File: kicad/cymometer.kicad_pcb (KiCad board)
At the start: 2 copper layers, 128.4 x 62 mm, 60 parts, among them IC1 ATMEGA8-P, P1 BNC, P2 CONN_2, P3 CONN_3X2, Q1 BC550, SW1 SW_PUSH, SW2 SPST, SW3 SW_PUSH, U1 7805, X1 20.48 MГц

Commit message: New commit
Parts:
- added REF**: Pin_Header_Straight_1x07, Pin_Headers:Pin_Header_Straight_1x07, F.Cu at (116.3, 22.2)
- added REF**: Pin_Header_Straight_1x13, Pin_Headers:Pin_Header_Straight_1x13, F.Cu at (116.4, 49.4)
- added REF**: Pin_Header_Angled_1x13, Pin_Headers:Pin_Header_Angled_1x13, F.Cu at (179.1, 50.8)
- added REF**: Pin_Header_Angled_1x07, Pin_Headers:Pin_Header_Angled_1x07, F.Cu at (179.1, 24.1)
- AFF1, AFF2, AFF3, AFF4, AFF5, AFF6, AFF7, AFF8, D3, D4, DD5, SW1, SW2, SW3: moved to F.Cu
- R11, R12, R13, R14, R15, R16, R17: moved to B.Cu
- moved SW3 110.9 mm to (169.2, 106.9)
- moved SW1 108.7 mm to (156.4, 106.9), turned to 90 degrees
- moved SW2 94.9 mm to (163.9, 26.6), turned to 180 degrees
- moved AFF8 90.3 mm to (162.8, 91.5), turned to 90 degrees
- moved D2 87.6 mm to (85.5, 21.9), turned to 270 degrees
- moved R15 84.5 mm to (171.7, 31.9), turned to 90 degrees
- moved P2 83.8 mm to (81.8, 21.8)
- moved R14 80.9 mm to (168.6, 31.9), turned to 90 degrees
- moved AFF7 79.6 mm to (162.8, 83.9), turned to 90 degrees
- moved R13 78.1 mm to (165.6, 31.9), turned to 90 degrees
- moved U1 75.4 mm to (93.5, 22.3), turned to 0 degrees
- moved R11 74.8 mm to (162.5, 31.9), turned to 90 degrees
- moved C10 74.7 mm to (33.9, 28.5), turned to 90 degrees
- moved R17 71.7 mm to (159.5, 31.9), turned to 90 degrees
- moved AFF6 68.9 mm to (162.8, 76.3), turned to 90 degrees
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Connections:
- AFF1 pad 3: Net-(AFF1-Pad3) -> (no net)
- AFF1 pad 8: (no net) -> Net-(AFF1-Pad8)
- AFF2 pad 3: Net-(AFF2-Pad3) -> (no net)
- AFF2 pad 8: (no net) -> Net-(AFF2-Pad8)
- AFF3 pad 3: Net-(AFF3-Pad3) -> (no net)
- AFF3 pad 8: (no net) -> Net-(AFF3-Pad8)
- AFF4 pad 3: Net-(AFF4-Pad3) -> (no net)
- AFF4 pad 8: (no net) -> Net-(AFF4-Pad8)
- AFF5 pad 3: Net-(AFF5-Pad3) -> (no net)
- AFF5 pad 8: (no net) -> Net-(AFF5-Pad8)
- AFF6 pad 3: Net-(AFF6-Pad3) -> (no net)
- AFF6 pad 8: (no net) -> Net-(AFF6-Pad8)
- AFF7 pad 3: Net-(AFF7-Pad3) -> (no net)
- AFF7 pad 8: (no net) -> Net-(AFF7-Pad8)
- AFF8 pad 3: Net-(AFF8-Pad3) -> (no net)
- AFF8 pad 8: (no net) -> Net-(AFF8-Pad8)
- DD5 pad 10: Net-(AFF1-Pad3) -> Net-(AFF1-Pad8)
- DD5 pad 2: Net-(AFF8-Pad3) -> Net-(AFF8-Pad8)
- DD5 pad 3: Net-(AFF7-Pad3) -> Net-(AFF7-Pad8)
- DD5 pad 4: Net-(AFF6-Pad3) -> Net-(AFF6-Pad8)
- DD5 pad 5: Net-(AFF5-Pad3) -> Net-(AFF5-Pad8)
- DD5 pad 6: Net-(AFF4-Pad3) -> Net-(AFF4-Pad8)
- DD5 pad 7: Net-(AFF3-Pad3) -> Net-(AFF3-Pad8)
- DD5 pad 9: Net-(AFF2-Pad3) -> Net-(AFF2-Pad8)
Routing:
- net Net-(DD2-Pad12): track 44.7 -> 120.6 mm, vias 1 -> 0
- net Net-(AFF7-Pad3): track 75.1 -> 0.00 mm
- net Net-(IC1-Pad17): track 89.6 -> 22.2 mm
- net Net-(DD1-Pad8): track 96.6 -> 30.5 mm
- net Net-(AFF1-Pad8): track 0.00 -> 55.6 mm
- net Net-(DD1-Pad1): track 26.1 -> 79.2 mm
- net Net-(IC1-Pad18): track 67.8 -> 16.6 mm
- net Net-(AFF8-Pad3): track 50.8 -> 0.00 mm
- net Net-(IC1-Pad19): track 58.2 -> 14.8 mm, vias 1 -> 0
- net Net-(AFF2-Pad3): track 39.2 -> 0.00 mm
- net Net-(AFF6-Pad3): track 38.7 -> 0.00 mm
- net Net-(AFF5-Pad3): track 34.3 -> 0.00 mm
- net Net-(IC1-Pad27): track 41.0 -> 6.73 mm, vias 1 -> 0
- net Net-(IC1-Pad23): track 40.8 -> 6.73 mm
- net Net-(DD4-Pad9): track 11.5 -> 44.4 mm
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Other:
- board size 128.4 x 62 mm -> 93.6 x 62 mm

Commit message: Add display board
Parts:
- removed the REF** at (116.3, 22.2)
- removed the REF** at (116.4, 49.4)
- added REF**: Socket_Strip_Straight_1x07, Socket_Strips:Socket_Strip_Straight_1x07, F.Cu at (116.4, 22.2)
- added REF**: Socket_Strip_Straight_1x12, Socket_Strips:Socket_Strip_Straight_1x13, F.Cu at (116.2, 49.4)
- REF**: value Pin_Header_Angled_1x13 -> Pin_Header_Angled_1x12
- moved SW2 92.7 mm to (162.6, 119.4)
- moved REF** 41.2 mm to (178.6, 91.9)
- moved REF** 40.6 mm to (178.6, 64.8)
- moved SW1 0.66 mm to (156.5, 107.6)
- moved SW3 0.66 mm to (169.2, 107.6)
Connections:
- AFF1 pad 3: (no net) -> Net-(AFF1-Pad3)
- AFF1 pad 8: Net-(AFF1-Pad8) -> (no net)
- AFF2 pad 3: (no net) -> Net-(AFF2-Pad3)
- AFF2 pad 8: Net-(AFF2-Pad8) -> (no net)
- AFF3 pad 3: (no net) -> Net-(AFF3-Pad3)
- AFF3 pad 8: Net-(AFF3-Pad8) -> (no net)
- AFF4 pad 3: (no net) -> Net-(AFF4-Pad3)
- AFF4 pad 8: Net-(AFF4-Pad8) -> (no net)
- AFF5 pad 3: (no net) -> Net-(AFF5-Pad3)
- AFF5 pad 8: Net-(AFF5-Pad8) -> (no net)
- AFF6 pad 3: (no net) -> Net-(AFF6-Pad3)
- AFF6 pad 8: Net-(AFF6-Pad8) -> (no net)
- AFF7 pad 3: (no net) -> Net-(AFF7-Pad3)
- AFF7 pad 8: Net-(AFF7-Pad8) -> (no net)
- AFF8 pad 3: (no net) -> Net-(AFF8-Pad3)
- AFF8 pad 8: Net-(AFF8-Pad8) -> (no net)
- DD5 pad 10: Net-(AFF1-Pad8) -> Net-(AFF1-Pad3)
- DD5 pad 2: Net-(AFF8-Pad8) -> Net-(AFF8-Pad3)
- DD5 pad 3: Net-(AFF7-Pad8) -> Net-(AFF7-Pad3)
- DD5 pad 4: Net-(AFF6-Pad8) -> Net-(AFF6-Pad3)
- DD5 pad 5: Net-(AFF5-Pad8) -> Net-(AFF5-Pad3)
- DD5 pad 6: Net-(AFF4-Pad8) -> Net-(AFF4-Pad3)
- DD5 pad 7: Net-(AFF3-Pad8) -> Net-(AFF3-Pad3)
- DD5 pad 9: Net-(AFF2-Pad8) -> Net-(AFF2-Pad3)
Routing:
- net Net-(AFF1-Pad3): track 0.00 -> 123.4 mm
- net Net-(IC1-Pad23): track 6.73 -> 87.0 mm
- net Net-(AFF2-Pad3): track 0.00 -> 79.7 mm
- net Net-(IC1-Pad27): track 6.73 -> 80.7 mm, vias 0 -> 1
- net Net-(IC1-Pad19): track 14.8 -> 85.5 mm
- net Net-(AFF3-Pad3): track 0.00 -> 65.7 mm
- net Net-(IC1-Pad24): track 6.73 -> 72.2 mm, vias 0 -> 1
- net Net-(AFF4-Pad3): track 0.00 -> 63.7 mm
- net Net-(IC1-Pad25): track 6.73 -> 67.1 mm, vias 0 -> 1
- net Net-(AFF5-Pad3): track 0.00 -> 60.1 mm, vias 0 -> 2
- net Net-(IC1-Pad28): track 6.73 -> 63.1 mm, vias 0 -> 1
- net Net-(IC1-Pad26): track 6.73 -> 62.7 mm
- net Net-(AFF1-Pad8): track 55.6 -> 0.00 mm
- net Net-(AFF6-Pad3): track 0.00 -> 51.0 mm
- net Net-(AFF7-Pad3): track 0.00 -> 48.6 mm, vias 0 -> 1
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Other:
- board size 93.6 x 62 mm -> 152.5 x 105.3 mm

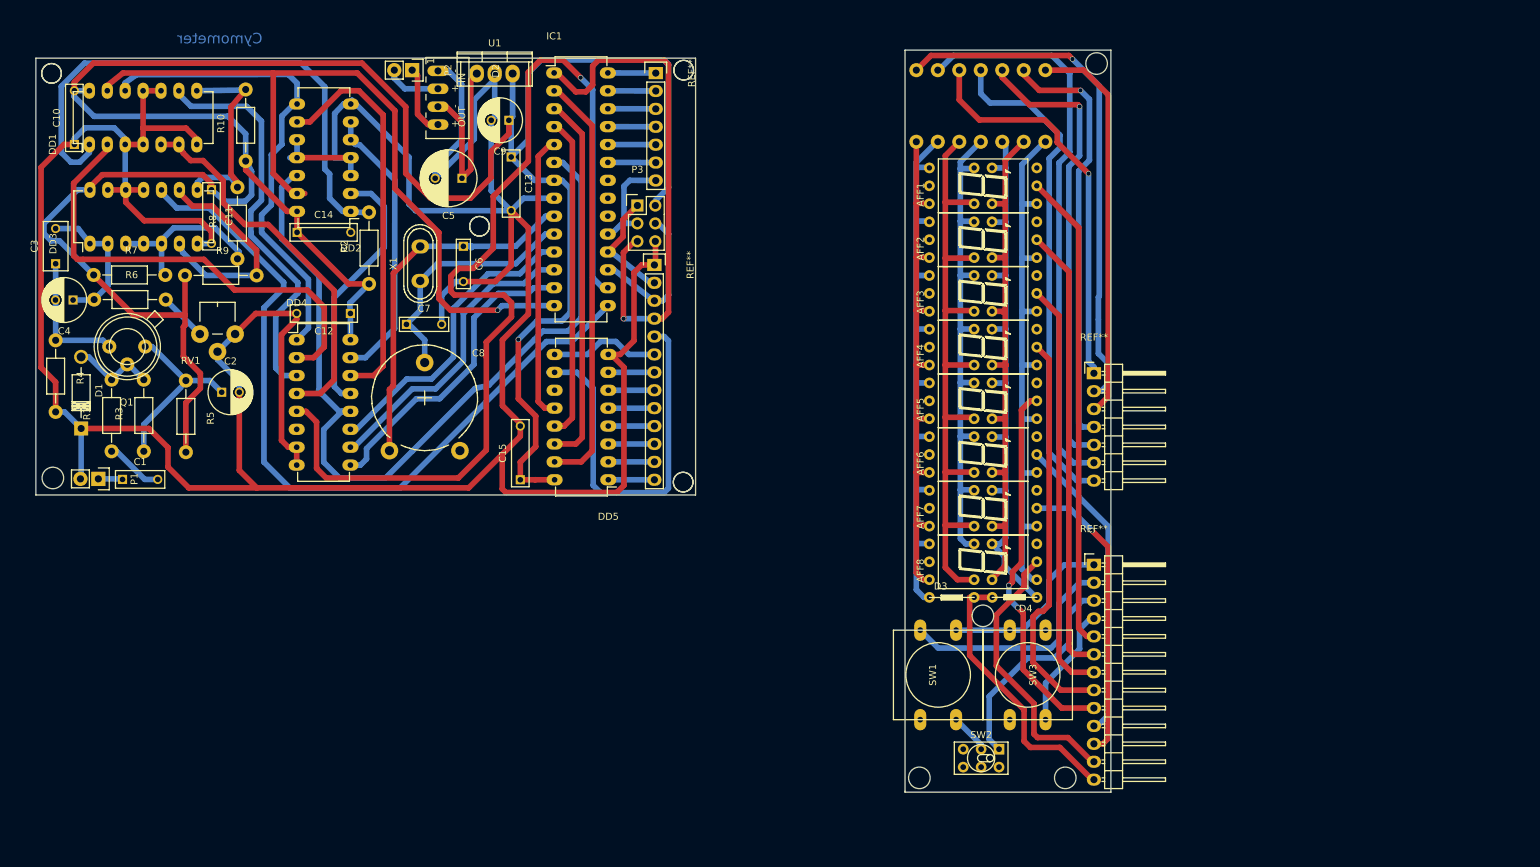
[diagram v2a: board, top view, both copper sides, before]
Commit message: End the tracing
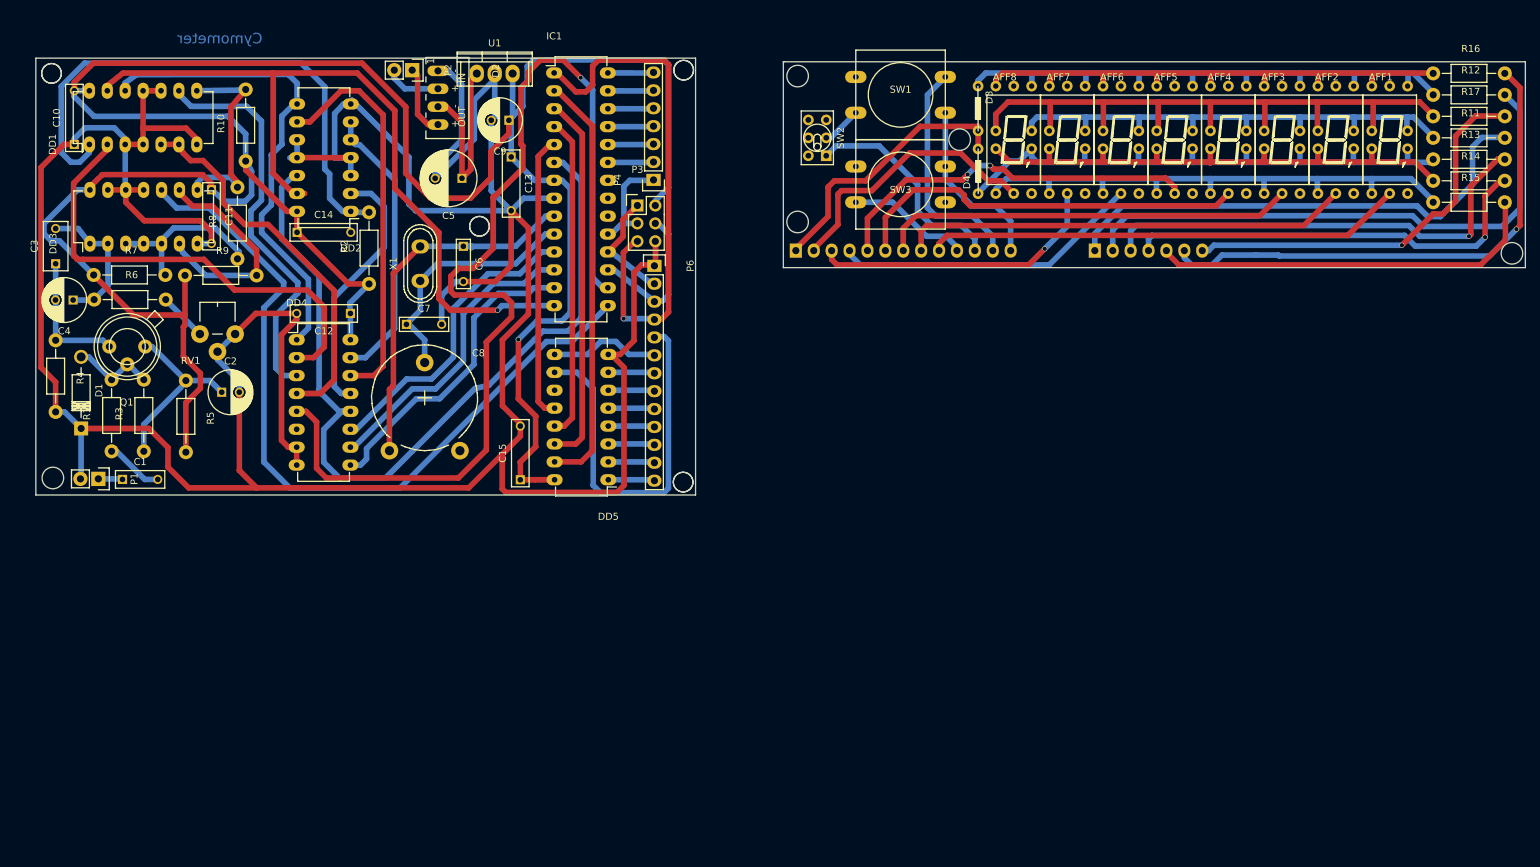
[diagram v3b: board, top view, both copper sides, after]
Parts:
- removed REF**: Pin_Header_Angled_1x07, Pin_Headers:Pin_Header_Angled_1x07
- removed REF**: Socket_Strip_Straight_1x07, Socket_Strips:Socket_Strip_Straight_1x07
- removed REF**: Socket_Strip_Straight_1x12, Socket_Strips:Socket_Strip_Straight_1x13
- removed REF**: Pin_Header_Angled_1x12, Pin_Headers:Pin_Header_Angled_1x13
- added P4: CONN_7, Socket_Strips:Socket_Strip_Straight_1x07, F.Cu at (116.1, 37.3)
- added P5: CONN_7, Pin_Headers:Pin_Header_Angled_1x07, B.Cu at (178.7, 47.4)
- added P6: CONN_13, Socket_Strips:Socket_Strip_Straight_1x13, F.Cu at (116.2, 49.5)
- added P7: CONN_13, Pin_Headers:Pin_Header_Angled_1x13, B.Cu at (136.3, 47.4)
- R11, R12, R13, R14, R15, R16, R17: moved to F.Cu
- moved SW2 91.0 mm to (139.3, 31.4), turned to 90 degrees
- moved SW1 82.5 mm to (151.1, 25.3), turned to 0 degrees
- moved R16 74.0 mm to (226.7, 22.2), turned to 0 degrees
- moved SW3 71.9 mm to (151.1, 38.0), turned to 180 degrees
- moved R12 70.6 mm to (226.7, 25.3), turned to 0 degrees
- moved D3 68.8 mm to (162.1, 27.8), turned to 270 degrees
- moved R17 67.3 mm to (226.7, 28.3), turned to 0 degrees
- moved R11 64.2 mm to (226.7, 31.4), turned to 0 degrees
- moved D4 61.3 mm to (162.1, 35.5), turned to 90 degrees
- moved R13 61.2 mm to (226.7, 34.4), turned to 0 degrees
- moved AFF8 60.0 mm to (167.2, 31.6), turned to 0 degrees
- moved R14 58.4 mm to (226.7, 37.5), turned to 0 degrees
- moved AFF1 58.1 mm to (220.5, 31.6), turned to 0 degrees
- moved R15 55.7 mm to (226.7, 40.5), turned to 0 degrees
- moved AFF7 53.6 mm to (174.8, 31.6), turned to 0 degrees
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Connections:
- DD5 pad 1: Net-(D3-Pad2) -> Net-(DD5-Pad1)
- DD5 pad 10: Net-(AFF1-Pad3) -> Net-(DD5-Pad10)
- DD5 pad 2: Net-(AFF8-Pad3) -> Net-(DD5-Pad2)
- DD5 pad 3: Net-(AFF7-Pad3) -> Net-(DD5-Pad3)
- DD5 pad 4: Net-(AFF6-Pad3) -> Net-(DD5-Pad4)
- DD5 pad 5: Net-(AFF5-Pad3) -> Net-(DD5-Pad5)
- DD5 pad 6: Net-(AFF4-Pad3) -> Net-(DD5-Pad6)
- DD5 pad 7: Net-(AFF3-Pad3) -> Net-(DD5-Pad7)
- DD5 pad 9: Net-(AFF2-Pad3) -> Net-(DD5-Pad9)
- R11 pad 2: Net-(IC1-Pad19) -> Net-(P5-Pad1)
- R12 pad 2: Net-(IC1-Pad23) -> Net-(P5-Pad2)
- R13 pad 2: Net-(IC1-Pad24) -> Net-(P5-Pad3)
- R14 pad 2: Net-(IC1-Pad25) -> Net-(P5-Pad4)
- R15 pad 2: Net-(IC1-Pad26) -> Net-(P5-Pad5)
- R16 pad 2: Net-(IC1-Pad27) -> Net-(P5-Pad6)
- R17 pad 2: Net-(IC1-Pad28) -> Net-(P5-Pad7)
- SW1 pad 1: Net-(IC1-Pad18) -> Net-(P7-Pad12)
- SW1 pad 2: GND -> Net-(P7-Pad13)
- SW2 pad 1: Net-(IC1-Pad17) -> Net-(P7-Pad11)
- SW2 pad 2: GND -> Net-(P7-Pad13)
- SW3 pad 1: Net-(IC1-Pad1) -> Net-(P7-Pad10)
- SW3 pad 2: GND -> Net-(P7-Pad13)
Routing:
- net Net-(P5-Pad2): track 0.00 -> 80.3 mm
- net Net-(IC1-Pad23): track 87.0 -> 6.73 mm
- net Net-(P5-Pad6): track 0.00 -> 74.0 mm, vias 0 -> 1
- net Net-(IC1-Pad27): track 80.7 -> 6.73 mm, vias 1 -> 0
- net Net-(IC1-Pad19): track 85.5 -> 14.8 mm
- net Net-(P5-Pad1): track 0.00 -> 70.7 mm
- net Net-(IC1-Pad24): track 72.2 -> 6.73 mm, vias 1 -> 0
- net Net-(P5-Pad3): track 0.00 -> 65.5 mm, vias 0 -> 1
- net Net-(IC1-Pad25): track 67.1 -> 6.73 mm, vias 1 -> 0
- net Net-(P5-Pad4): track 0.00 -> 60.4 mm, vias 0 -> 1
- net Net-(P5-Pad7): track 0.00 -> 56.3 mm, vias 0 -> 1
- net Net-(IC1-Pad28): track 63.1 -> 6.73 mm, vias 1 -> 0
- net Net-(IC1-Pad26): track 62.7 -> 6.73 mm
- net Net-(P5-Pad5): track 0.00 -> 55.9 mm
- net Net-(AFF1-Pad3): track 123.4 -> 67.9 mm
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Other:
- board size 152.5 x 105.3 mm -> 211.3 x 62 mm

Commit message: change switch
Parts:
- removed SW2: SPST, Buttons_Switches_ThroughHole:SW_NKK_G1xJP
- removed SW3: SW_PUSH, Buttons_Switches_ThroughHole:SW_PUSH-12mm
- P6: value CONN_13 -> CONN_12; footprint Socket_Strips:Socket_Strip_Straight_1x13 -> Socket_Strips:Socket_Strip_Straight_1x12
- P7: value CONN_13 -> CONN_12; footprint Pin_Headers:Pin_Header_Angled_1x13 -> Pin_Headers:Pin_Header_Angled_1x12
- SW1: value SW_PUSH -> switch_3; footprint Buttons_Switches_ThroughHole:SW_PUSH-12mm -> cymometer:switch3
- moved P6 28.5 mm to (116.7, 78.0), turned to 90 degrees
- moved AFF1 20.3 mm to (200.5, 28.9)
- moved AFF2 20.3 mm to (192.8, 28.9)
- moved AFF3 20.3 mm to (185.2, 28.9)
- moved AFF4 20.3 mm to (177.6, 28.9)
- moved AFF5 20.3 mm to (170.0, 28.9)
- moved AFF6 20.3 mm to (162.3, 28.9)
- moved AFF7 20.3 mm to (154.7, 28.9)
- moved D3 20.3 mm to (142.1, 25.0)
- moved D4 20.3 mm to (142.1, 32.7)
- moved R11 20.3 mm to (206.6, 28.6)
- moved R12 20.3 mm to (206.6, 22.5)
- moved R13 20.3 mm to (206.6, 31.6)
- moved R14 20.3 mm to (206.6, 34.7)
- moved R15 20.3 mm to (206.6, 37.7)
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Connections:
- P6 pad 1: GND -> Net-(DD5-Pad1)
- P6 pad 10: Net-(DD5-Pad4) -> Net-(IC1-Pad17)
- P6 pad 11: Net-(DD5-Pad3) -> Net-(IC1-Pad18)
- P6 pad 12: Net-(DD5-Pad2) -> GND
- P6 pad 2: Net-(IC1-Pad18) -> Net-(DD5-Pad2)
- P6 pad 3: Net-(IC1-Pad17) -> Net-(DD5-Pad3)
- P6 pad 4: Net-(IC1-Pad1) -> Net-(DD5-Pad4)
- P6 pad 5: Net-(DD5-Pad10) -> Net-(DD5-Pad5)
- P6 pad 6: Net-(DD5-Pad9) -> Net-(DD5-Pad6)
- P6 pad 8: Net-(DD5-Pad6) -> Net-(DD5-Pad9)
- P6 pad 9: Net-(DD5-Pad5) -> Net-(DD5-Pad10)
- SW1 pad 2: Net-(P7-Pad13) -> Net-(P7-Pad11)
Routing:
- net Net-(AFF5-Pad3): track 53.4 -> 86.2 mm, vias 2 -> 0
- net Net-(P7-Pad13): track 31.0 -> 0.00 mm
- net Net-(P7-Pad10): track 17.5 -> 38.3 mm
- net Net-(AFF8-Pad3): track 39.2 -> 19.5 mm
- net Net-(AFF7-Pad3): track 41.9 -> 61.2 mm, vias 1 -> 0
- net Net-(AFF4-Pad3): track 57.0 -> 38.0 mm
- net Net-(IC1-Pad1): track 75.0 -> 56.0 mm, vias 1 -> 0
- net Net-(P5-Pad4): track 60.4 -> 43.8 mm
- net Net-(P5-Pad3): track 65.5 -> 49.3 mm
- net Net-(AFF2-Pad3): track 63.8 -> 47.8 mm
- net Net-(AFF3-Pad3): track 59.0 -> 43.0 mm
- net Net-(P5-Pad2): track 80.3 -> 64.4 mm
- net Net-(AFF1-Pad3): track 67.9 -> 52.6 mm, vias 0 -> 1
- net Net-(P5-Pad6): track 74.0 -> 58.7 mm
- net Net-(P5-Pad7): track 56.3 -> 41.2 mm
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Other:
- board size 211.3 x 62 mm -> 190.9 x 62.4 mm

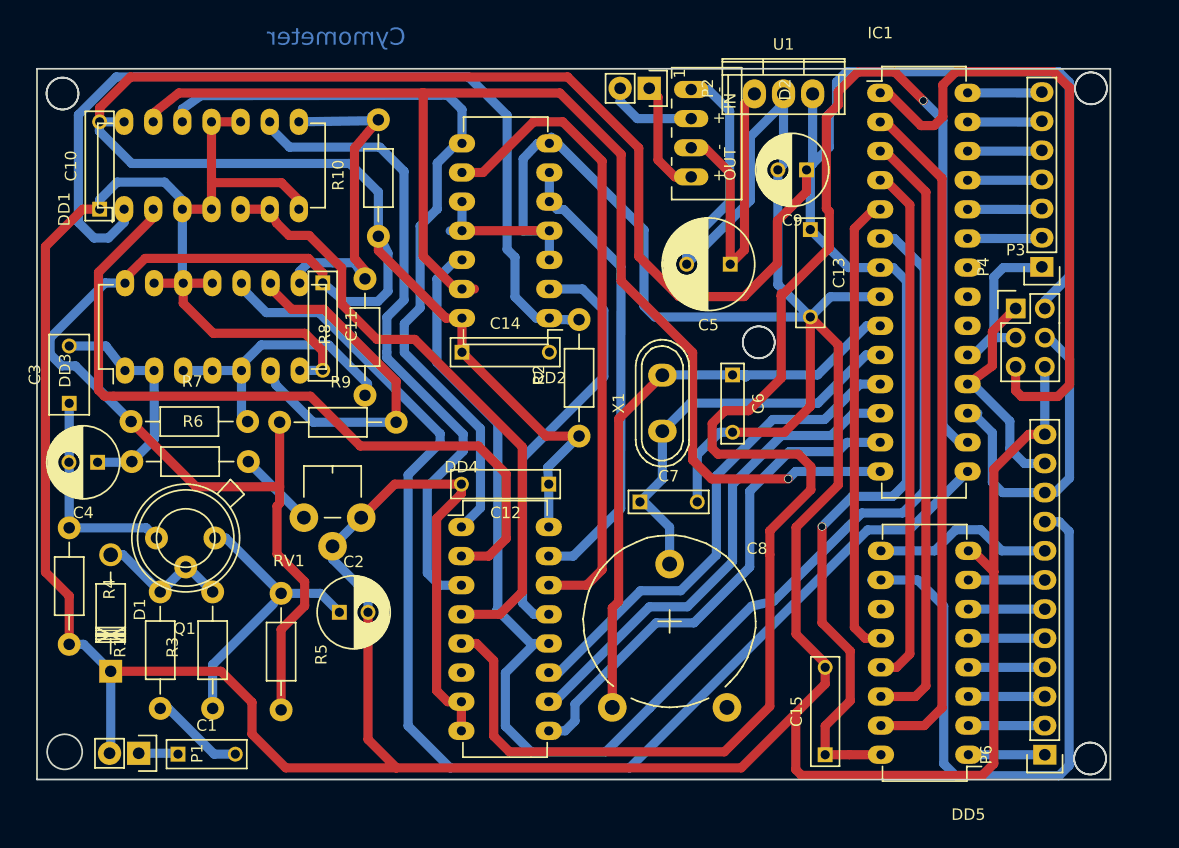
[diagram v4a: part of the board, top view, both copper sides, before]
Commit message: Add mask to board
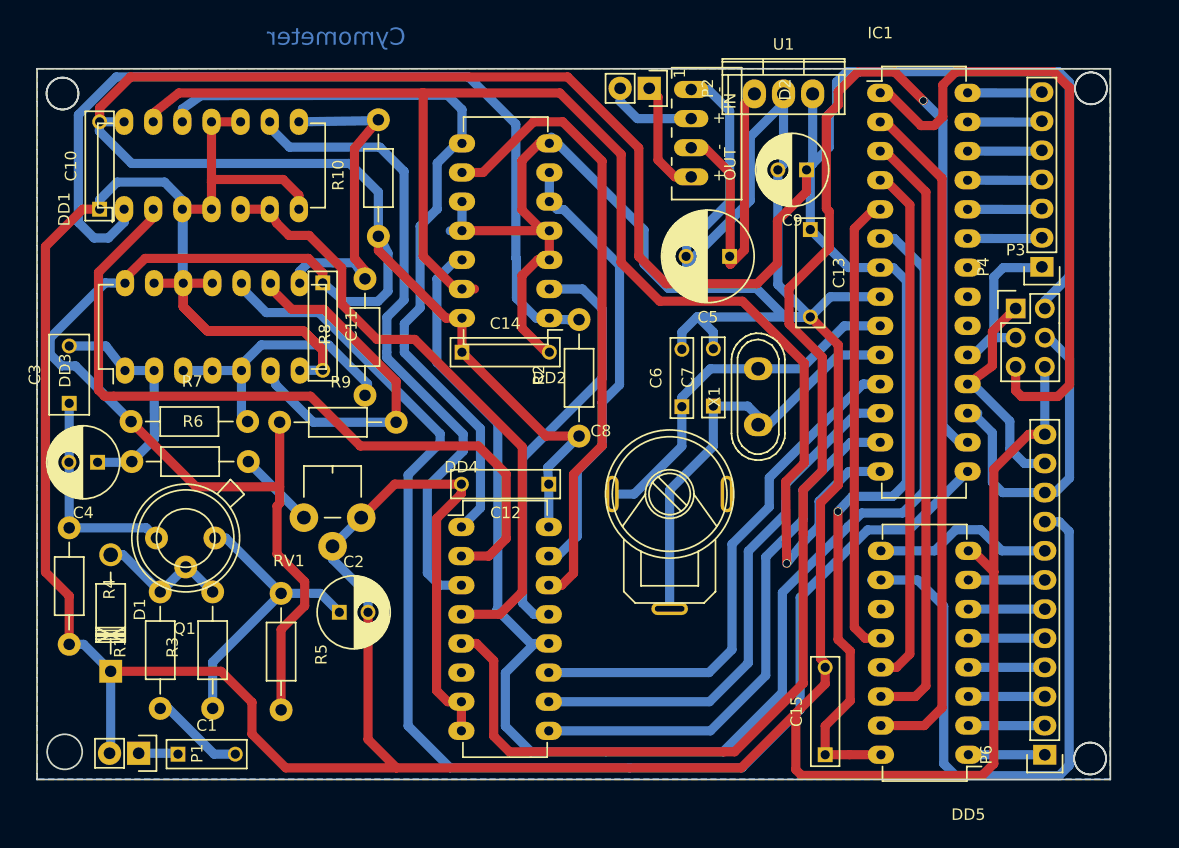
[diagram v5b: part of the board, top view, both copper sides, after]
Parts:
- C8: footprint Potentiometers:Potentiometer_Trimmer-Piher_PT15-V12-5_horizontal -> cymometer:кпк-мп
- moved C8 19.3 mm to (84.0, 55.2)
- moved C7 10.5 mm to (87.8, 47.6), turned to 90 degrees
- moved X1 8.38 mm to (91.7, 46.8)
- moved C6 5.22 mm to (85.1, 47.6), turned to 90 degrees
- moved C5 0.69 mm to (89.2, 34.5)
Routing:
- net GND: track 491.9 -> 517.6 mm, vias 0 -> 1
- net Net-(C6-Pad1): track 53.0 -> 33.0 mm
- net Net-(DD1-Pad13): track 111.5 -> 125.0 mm
- net Net-(DD4-Pad5): track 146.2 -> 136.5 mm
- net Net-(DD3-Pad10): track 110.6 -> 116.4 mm
- net Net-(DD2-Pad12): track 120.6 -> 125.8 mm
- net Net-(DD4-Pad10): track 43.7 -> 48.0 mm
- net Net-(DD4-Pad11): track 43.8 -> 48.0 mm
- net Net-(DD4-Pad9): track 44.4 -> 47.3 mm
- net VCC: track 375.1 -> 373.1 mm
- net Net-(DD2-Pad9): track 56.3 -> 55.0 mm
- net Net-(C2-Pad1): track 24.8 -> 26.0 mm
- net Net-(C7-Pad1): track 35.4 -> 36.5 mm
- net Net-(DD2-Pad5): track 40.2 -> 39.3 mm
- net Net-(C5-Pad1): track 28.0 -> 28.7 mm
- added copper zone on B.Cu, net GND
- added copper zone on F.Cu, net GND
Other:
- outline, holes or cut-outs redrawn
